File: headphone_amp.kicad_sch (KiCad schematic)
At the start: 0 parts

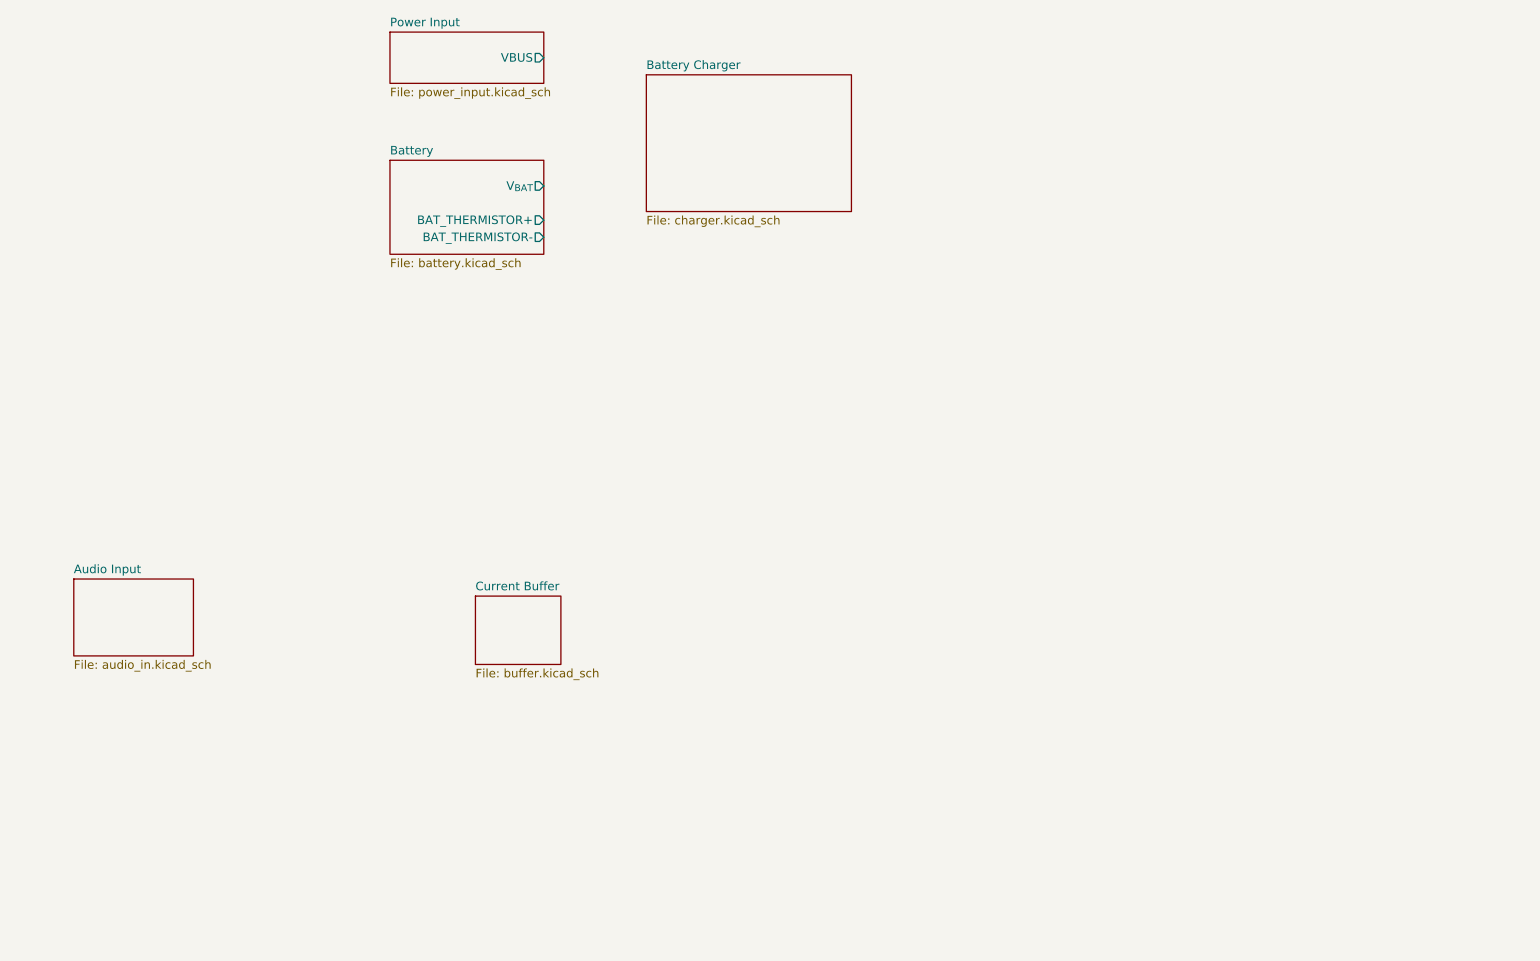
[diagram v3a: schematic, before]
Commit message: Added notes and started work on boost converter.
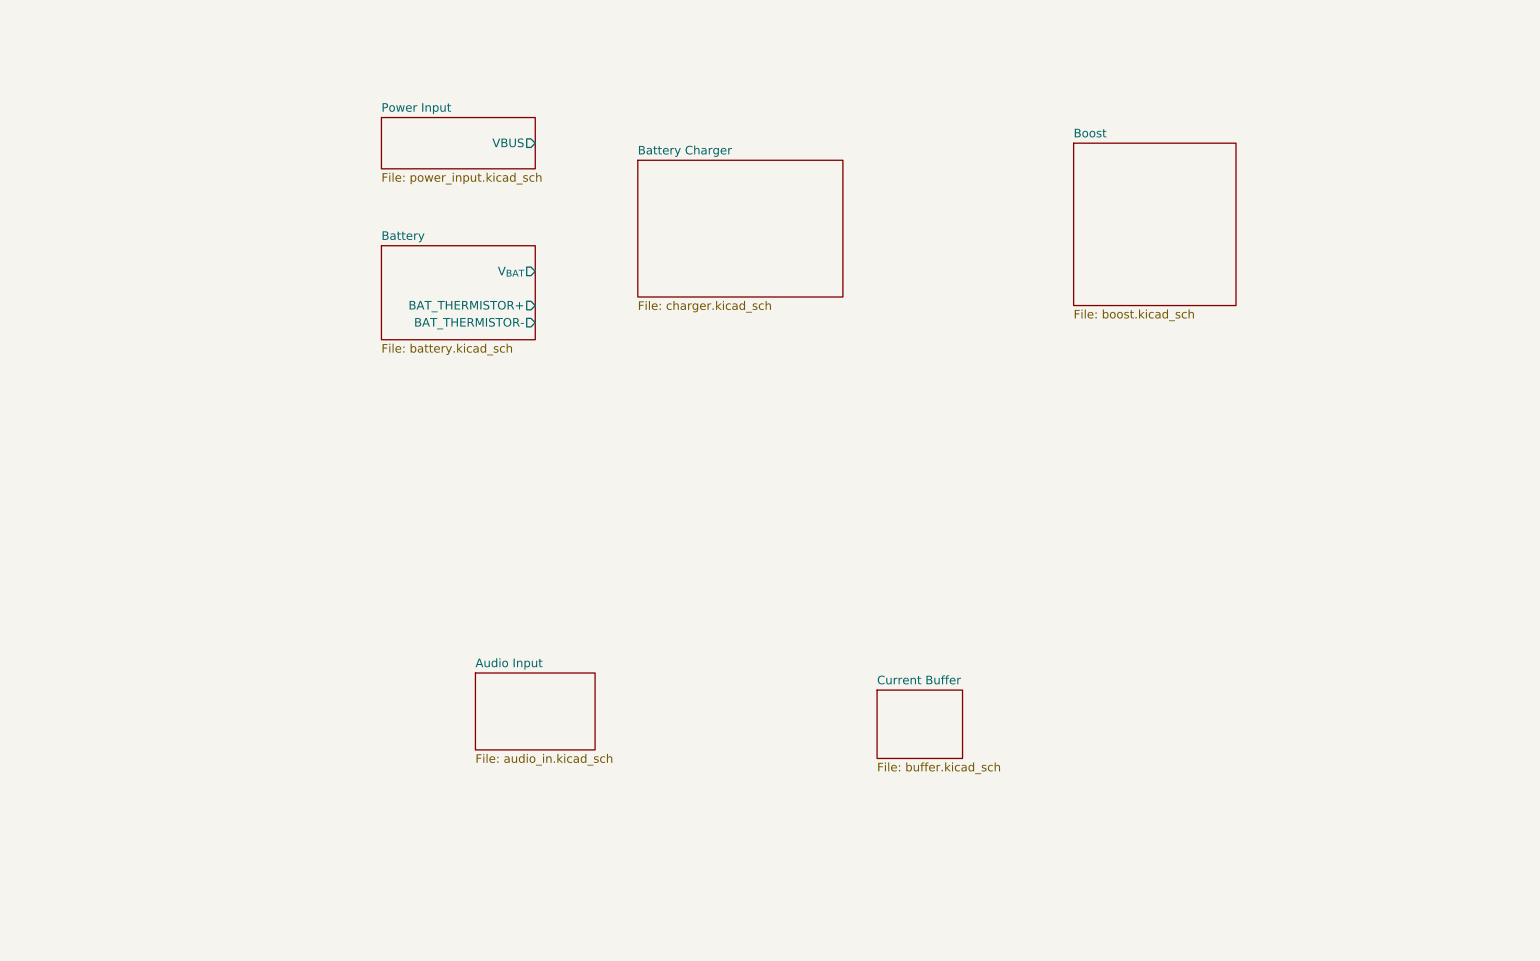
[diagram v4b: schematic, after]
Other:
- added sheet Boost (boost.kicad_sch)
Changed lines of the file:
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@@
 	(paper "A4")
 	(sheet
-		(at 96.52 29.21)
+		(at 95.25 41.91)
 		(size 22.86 7.62)
 		(exclude_from_sim no)
@@
 		)
 		(property "Sheetname" "Power Input"
-			(at 96.52 28.4984 0)
+			(at 95.25 41.1984 0)
 			(show_name no)
 			(do_not_autoplace no)
@@
 		)
 		(property "Sheetfile" "power_input.kicad_sch"
-			(at 96.52 37.4146 0)
+			(at 95.25 50.1146 0)
 			(show_name no)
 			(do_not_autoplace no)
@@
 		)
 		(pin "VBUS" output
-			(at 119.38 33.02 0)
+			(at 118.11 45.72 0)
 			(effects
 				(font
@@
 	)
 	(sheet
-		(at 96.52 48.26)
+		(at 198.12 45.72)
+		(size 24.13 24.13)
+		(exclude_from_sim no)
+		(in_bom yes)
+		(on_board yes)
+		(dnp no)
+		(fields_autoplaced yes)
+		(stroke
+			(width 0.1524)
+			(type solid)
+		)
+		(fill
+			(color 0 0 0 0)
+		)
+		(property "Sheetname" "Boost"
+			(at 198.12 45.0084 0)
+			(show_name no)
+			(do_not_autoplace no)
+			(effects
+				(font
+					(size 1.27 1.27)
+				)
+				(justify left bottom)
+			)
+		)
+		(property "Sheetfile" "boost.kicad_sch"
+			(at 198.12 70.4346 0)
+			(show_name no)
+			(do_not_autoplace no)
+			(effects
+				(font
+					(size 1.27 1.27)
+				)
+				(justify left top)
+			)
+		)
+		(instances
+			(project "headphone_amp"
+				(path "/62ffec33-ae93-49a8-bfe6-566578dd8e82"
+					(page "7")
+				)
+			)
+		)
+	)
+	(sheet
+		(at 95.25 60.96)
 		(size 22.86 13.97)
 		(exclude_from_sim no)
@@
 		)
 		(property "Sheetname" "Battery"
-			(at 96.52 47.5484 0)
+			(at 95.25 60.2484 0)
 			(show_name no)
 			(do_not_autoplace no)
@@
 		)
 		(property "Sheetfile" "battery.kicad_sch"
-			(at 96.52 62.8146 0)
+			(at 95.25 75.5146 0)
 			(show_name no)
 			(do_not_autoplace no)
@@
 		)
 		(pin "BAT_THERMISTOR+" output
-			(at 119.38 57.15 0)
+			(at 118.11 69.85 0)
 			(effects
 				(font
@@
 		)
 		(pin "BAT_THERMISTOR-" output
-			(at 119.38 59.69 0)
+			(at 118.11 72.39 0)
 			(effects
 				(font
@@
 		)
 		(pin "V_{BAT}" output
-			(at 119.38 52.07 0)
+			(at 118.11 64.77 0)
 			(effects
 				(font
@@
 	)
 	(sheet
-		(at 134.62 35.56)
+		(at 133.35 48.26)
 		(size 30.48 20.32)
 		(exclude_from_sim no)
@@
 		)
 		(property "Sheetname" "Battery Charger"
-			(at 134.62 34.8484 0)
+			(at 133.35 47.5484 0)
 			(show_name no)
 			(do_not_autoplace no)
@@
 		)
 		(property "Sheetfile" "charger.kicad_sch"
-			(at 134.62 56.4646 0)
+			(at 133.35 69.1646 0)
 			(show_name no)
 			(do_not_autoplace no)
@@
 	)
 	(sheet
-		(at 109.22 113.03)
+		(at 168.91 127)
 		(size 12.7 10.16)
 		(exclude_from_sim no)
@@
 		)
 		(property "Sheetname" "Current Buffer"
-			(at 109.22 112.3184 0)
+			(at 168.91 126.2884 0)
 			(show_name no)
 			(do_not_autoplace no)
@@
 		)
 		(property "Sheetfile" "buffer.kicad_sch"
-			(at 109.22 123.7746 0)
+			(at 168.91 137.7446 0)
 			(show_name no)
 			(do_not_autoplace no)
@@
 	)
 	(sheet
-		(at 49.53 110.49)
+		(at 109.22 124.46)
 		(size 17.78 11.43)
 		(exclude_from_sim no)
@@
 		)
 		(property "Sheetname" "Audio Input"
-			(at 49.53 109.7784 0)
+			(at 109.22 123.7484 0)
 			(show_name no)
 			(do_not_autoplace no)
@@
 		)
 		(property "Sheetfile" "audio_in.kicad_sch"
-			(at 49.53 122.5046 0)
-			(show_name no)
-			(do_not_autoplace no)
+			(at 109.22 136.4746 0)
+			(show_name no)
+			(do_not_autoplace no)

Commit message: Implemented boost stage and now working on schematics for current buffers and rail splitter.
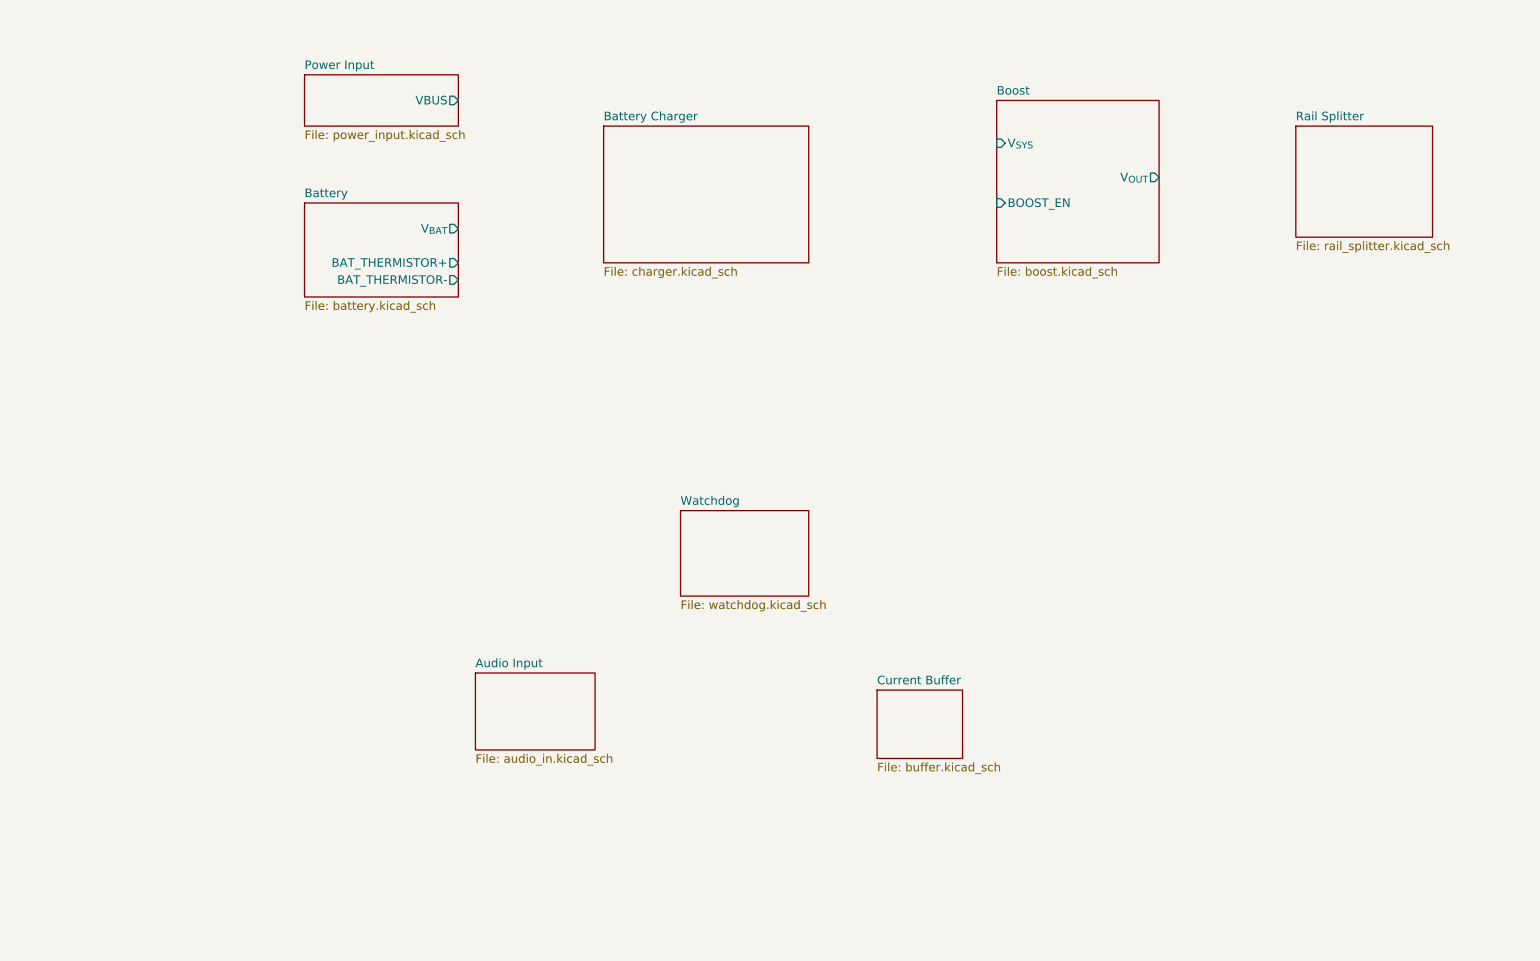
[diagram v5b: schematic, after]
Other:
- added sheet Rail Splitter (rail_splitter.kicad_sch)
- added sheet Watchdog (watchdog.kicad_sch)
- sheet Boost ports: added BOOST_EN, V_{OUT}, V_{SYS}; removed none
- title: (none) -> ${PROJECT_NAME}
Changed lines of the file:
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@@
 	(generator_version "10.0")
 	(paper "A4")
-	(sheet
-		(at 95.25 41.91)
+	(title_block
+		(title "${PROJECT_NAME}")
+		(date "2026-08-25")
+		(rev "${REVISION}")
+		(comment 1 "${PCBA_IPN}")
+	)
+	(sheet
+		(at 83.82 35.56)
 		(size 22.86 7.62)
 		(exclude_from_sim no)
@@
 		)
 		(property "Sheetname" "Power Input"
-			(at 95.25 41.1984 0)
+			(at 83.82 34.8484 0)
 			(show_name no)
 			(do_not_autoplace no)
@@
 		)
 		(property "Sheetfile" "power_input.kicad_sch"
-			(at 95.25 50.1146 0)
+			(at 83.82 43.7646 0)
 			(show_name no)
 			(do_not_autoplace no)
@@
 		)
 		(pin "VBUS" output
-			(at 118.11 45.72 0)
+			(at 106.68 39.37 0)
 			(effects
 				(font
@@
 	)
 	(sheet
-		(at 198.12 45.72)
+		(at 231.14 43.18)
+		(size 20.32 16.51)
+		(exclude_from_sim no)
+		(in_bom yes)
+		(on_board yes)
+		(dnp no)
+		(fields_autoplaced yes)
+		(stroke
+			(width 0.1524)
+			(type solid)
+		)
+		(fill
+			(color 0 0 0 0)
+		)
+		(property "Sheetname" "Rail Splitter"
+			(at 231.14 42.4684 0)
+			(show_name no)
+			(do_not_autoplace no)
+			(effects
+				(font
+					(size 1.27 1.27)
+				)
+				(justify left bottom)
+			)
+		)
+		(property "Sheetfile" "rail_splitter.kicad_sch"
+			(at 231.14 60.2746 0)
+			(show_name no)
+			(do_not_autoplace no)
+			(effects
+				(font
+					(size 1.27 1.27)
+				)
+				(justify left top)
+			)
+		)
+		(instances
+			(project "headphone_amp"
+				(path "/62ffec33-ae93-49a8-bfe6-566578dd8e82"
+					(page "9")
+				)
+			)
+		)
+	)
+	(sheet
+		(at 186.69 39.37)
 		(size 24.13 24.13)
 		(exclude_from_sim no)
@@
 		)
 		(property "Sheetname" "Boost"
-			(at 198.12 45.0084 0)
+			(at 186.69 38.6584 0)
 			(show_name no)
 			(do_not_autoplace no)
@@
 		)
 		(property "Sheetfile" "boost.kicad_sch"
-			(at 198.12 70.4346 0)
-			(show_name no)
-			(do_not_autoplace no)
-			(effects
-				(font
-					(size 1.27 1.27)
-				)
-				(justify left top)
+			(at 186.69 64.0846 0)
+			(show_name no)
+			(do_not_autoplace no)
+			(effects
+				(font
+					(size 1.27 1.27)
+				)
+				(justify left top)
+			)
+		)
+		(pin "V_{OUT}" output
+			(at 210.82 50.8 0)
+			(effects
+				(font
+					(size 1.27 1.27)
+				)
+				(justify right)
+			)
+		)
+		(pin "BOOST_EN" input
+			(at 186.69 54.61 180)
+			(effects
+				(font
+					(size 1.27 1.27)
+				)
+				(justify left)
+			)
+		)
+		(pin "V_{SYS}" input
+			(at 186.69 45.72 180)
+			(effects
+				(font
+					(size 1.27 1.27)
+				)
+				(justify left)
 			)
 		)
@@
 	)
 	(sheet
-		(at 95.25 60.96)
+		(at 83.82 54.61)
 		(size 22.86 13.97)
 		(exclude_from_sim no)
@@
 		)
 		(property "Sheetname" "Battery"
-			(at 95.25 60.2484 0)
+			(at 83.82 53.8984 0)
 			(show_name no)
 			(do_not_autoplace no)
@@
 		)
 		(property "Sheetfile" "battery.kicad_sch"
-			(at 95.25 75.5146 0)
+			(at 83.82 69.1646 0)
 			(show_name no)
 			(do_not_autoplace no)
@@
 		)
 		(pin "BAT_THERMISTOR+" output
-			(at 118.11 69.85 0)
+			(at 106.68 63.5 0)
 			(effects
 				(font
@@
 		)
 		(pin "BAT_THERMISTOR-" output
-			(at 118.11 72.39 0)
+			(at 106.68 66.04 0)
 			(effects
 				(font
@@
 		)
 		(pin "V_{BAT}" output
-			(at 118.11 64.77 0)
+			(at 106.68 58.42 0)
 			(effects
 				(font
@@
 	)
 	(sheet
-		(at 133.35 48.26)
+		(at 128.27 43.18)
 		(size 30.48 20.32)
 		(exclude_from_sim no)
@@
 		)
 		(property "Sheetname" "Battery Charger"
-			(at 133.35 47.5484 0)
+			(at 128.27 42.4684 0)
 			(show_name no)
 			(do_not_autoplace no)
@@
 		)
 		(property "Sheetfile" "charger.kicad_sch"
-			(at 133.35 69.1646 0)
+			(at 128.27 64.0846 0)
 			(show_name no)
 			(do_not_autoplace no)
@@
 				)
 			)
+		)
+	)
+	(sheet
+		(at 139.7 100.33)
+		(size 19.05 12.7)
+		(exclude_from_sim no)
+		(in_bom yes)
+		(on_board yes)
+		(dnp no)
+		(fields_autoplaced yes)
+		(stroke
+			(width 0.1524)
+			(type solid)
+		)
+		(fill
+			(color 0 0 0 0)
+		)
+		(property "Sheetname" "Watchdog"
+			(at 139.7 99.6184 0)
+			(show_name no)
+			(do_not_autoplace no)
+			(effects
+				(font
+					(size 1.27 1.27)
+				)
+				(justify left bottom)
+			)
+		)
+		(property "Sheetfile" "watchdog.kicad_sch"
+			(at 139.7 113.6146 0)
+			(show_name no)
+			(do_not_autoplace no)
+			(effects
+				(font
+					(size 1.27 1.27)
+				)
+				(justify left top)
+			)
+		)
+		(instances
+			(project "headphone_amp"
+				(path "/62ffec33-ae93-49a8-bfe6-566578dd8e82"
+					(page "8")
+				)
+			)

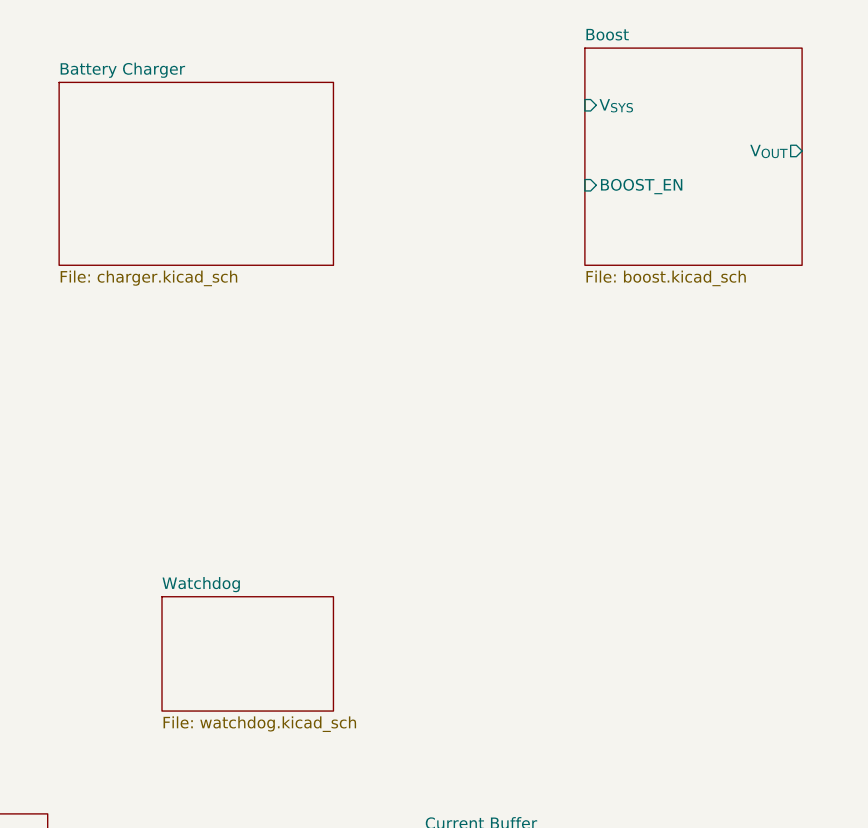
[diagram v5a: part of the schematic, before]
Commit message: Finalizing watchdog and boost circuit.
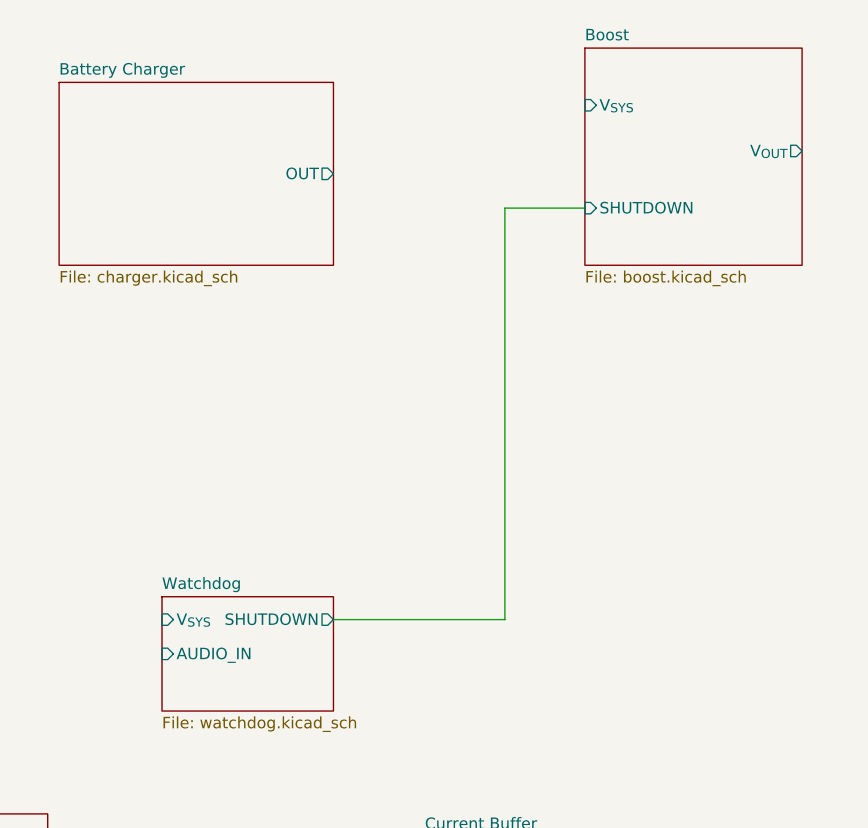
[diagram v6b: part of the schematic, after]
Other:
- sheet Battery Charger ports: added OUT; removed none
- sheet Boost ports: added SHUTDOWN; removed BOOST_EN
- sheet Watchdog ports: added AUDIO_IN, SHUTDOWN, V_{SYS}; removed none
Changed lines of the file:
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@@
 		(comment 1 "${PCBA_IPN}")
+	)
+	(wire
+		(pts
+			(xy 177.8 102.87) (xy 177.8 57.15)
+		)
+		(stroke
+			(width 0)
+			(type default)
+		)
+	)
+	(wire
+		(pts
+			(xy 177.8 57.15) (xy 186.69 57.15)
+		)
+		(stroke
+			(width 0)
+			(type default)
+		)
+	)
+	(wire
+		(pts
+			(xy 158.75 102.87) (xy 177.8 102.87)
+		)
+		(stroke
+			(width 0)
+			(type default)
+		)
 	)
 	(sheet
@@
 			)
 		)
-		(pin "BOOST_EN" input
-			(at 186.69 54.61 180)
-			(effects
-				(font
-					(size 1.27 1.27)
-				)
-				(justify left)
-			)
-		)
 		(pin "V_{SYS}" input
 			(at 186.69 45.72 180)
@@
 			)
 		)
+		(pin "SHUTDOWN" input
+			(at 186.69 57.15 180)
+			(effects
+				(font
+					(size 1.27 1.27)
+				)
+				(justify left)
+			)
+		)
 		(instances
 			(project "headphone_amp"
@@
 			)
 		)
+		(pin "OUT" output
+			(at 158.75 53.34 0)
+			(effects
+				(font
+					(size 1.27 1.27)
+				)
+				(justify right)
+			)
+		)
 		(instances
 			(project "headphone_amp"
@@
 			)
 		)
+		(pin "AUDIO_IN" input
+			(at 139.7 106.68 180)
+			(effects
+				(font
+					(size 1.27 1.27)
+				)
+				(justify left)
+			)
+		)
+		(pin "SHUTDOWN" output
+			(at 158.75 102.87 0)
+			(effects
+				(font
+					(size 1.27 1.27)
+				)
+				(justify right)
+			)
+		)
+		(pin "V_{SYS}" input
+			(at 139.7 102.87 180)
+			(effects
+				(font
+					(size 1.27 1.27)
+				)
+				(justify left)
+			)
+		)
